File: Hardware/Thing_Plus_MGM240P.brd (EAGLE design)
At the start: 22.9 x 58.4 mm, 176 parts, among them J1 THING_PLUS_LOGICAL, J2 USB Female Type C Connector, J3 QWIIC_RIGHT_ANGLE, J5 MICRO-SDFRICTION, Q1 20V/4.2A/52mΩ/1.4W, U1 MGM240P, U2 XC6222B331MR-G, U3 EFM32GG12B410F1024GL120, U4 MCP73831, U5 MAX17048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

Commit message: Fix air wire
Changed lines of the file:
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@@
 <wire x1="4.1569" y1="15.49" x2="4.0259" y2="15.621" width="0.254" layer="16"/>
 <via x="4.0259" y="15.621" extent="1-16" drill="0.3048"/>
-<via x="0.6604" y="8.0772" extent="1-16" drill="0.3048"/>
+<via x="3.4544" y="6.8072" extent="1-16" drill="0.3048"/>
 <contactref element="C1" pad="1"/>
 <wire x1="4.58" y1="12.7" x2="4.58" y2="15.0669" width="0.254" layer="1"/>
 <wire x1="4.58" y1="15.0669" x2="4.0259" y2="15.621" width="0.254" layer="1"/>
-<wire x1="1.778" y1="7.2517" x2="1.4859" y2="7.2517" width="0.127" layer="16"/>
-<wire x1="1.4859" y1="7.2517" x2="0.6604" y2="8.0772" width="0.127" layer="16"/>
+<wire x1="3.4544" y1="6.8072" x2="2.5654" y2="6.8072" width="0.127" layer="16"/>
+<wire x1="2.5654" y1="6.8072" x2="2.1209" y2="7.2517" width="0.127" layer="16"/>
+<wire x1="1.778" y1="7.2517" x2="2.1209" y2="7.2517" width="0.127" layer="16"/>
 <contactref element="U3" pad="L4"/>
 <contactref element="U3" pad="G3"/>
@@
 <contactref element="R19" pad="2"/>
 <wire x1="6.215" y1="25.4" x2="6.215" y2="26.67" width="0.127" layer="1"/>
-<wire x1="3.81" y1="9.398" x2="1.778" y2="7.2517" width="0" layer="19" extent="16-16"/>
 </signal>
 <signal name="V_USB">

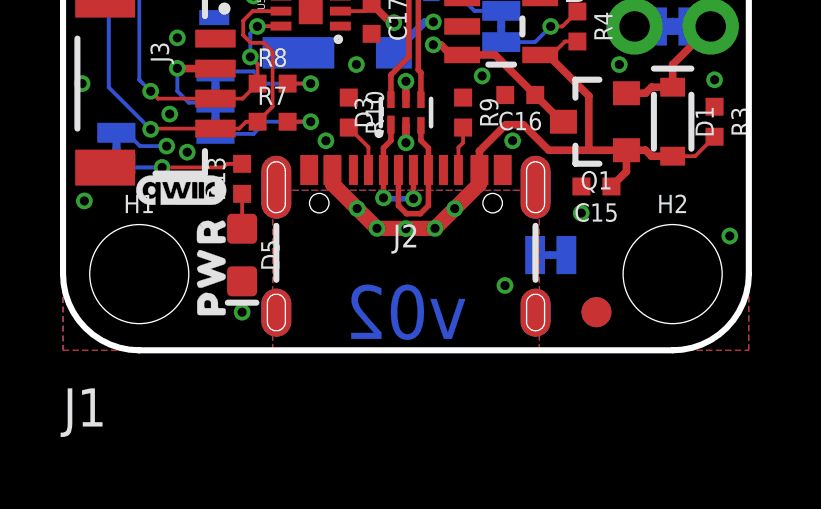
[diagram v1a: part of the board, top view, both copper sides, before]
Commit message: Update revision number to v10
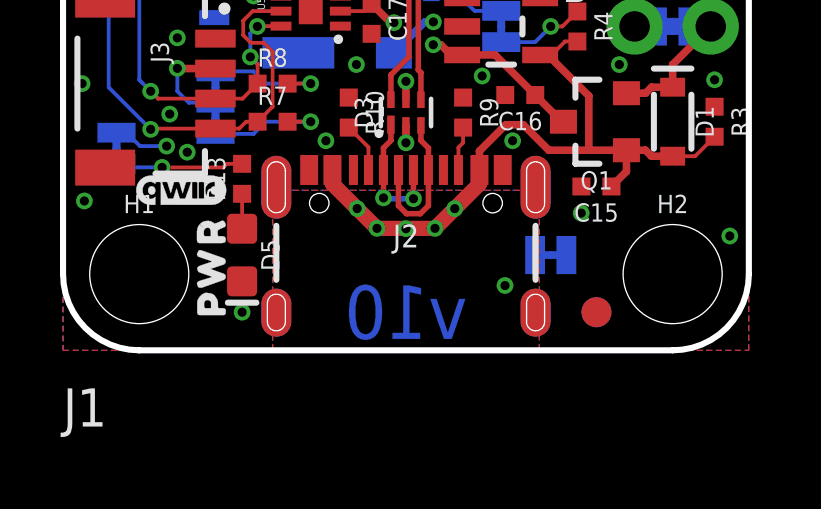
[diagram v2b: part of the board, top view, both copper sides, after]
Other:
- board text added: "v10"
- board text removed: "v02"
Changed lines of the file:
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@@
 <rectangle x1="16.891" y1="57.023" x2="17.272" y2="57.15" layer="41"/>
 <rectangle x1="16.891" y1="56.007" x2="17.272" y2="56.134" layer="41"/>
-<text x="11.43" y="1.27" size="1.778" layer="16" font="vector" ratio="15" rot="MR0" align="center">v02</text>
+<text x="11.43" y="1.27" size="1.778" layer="16" font="vector" ratio="15" rot="MR0" align="center">v10</text>
 <dimension x1="0" y1="0" x2="2.54" y2="0" x3="1.27" y3="-2.54" textsize="1.27" textratio="15" layer="47" unit="inch"/>
 <dimension x1="0" y1="0" x2="11.43" y2="0" x3="5.715" y3="-6.35" textsize="1.27" textratio="15" layer="47" unit="inch"/>

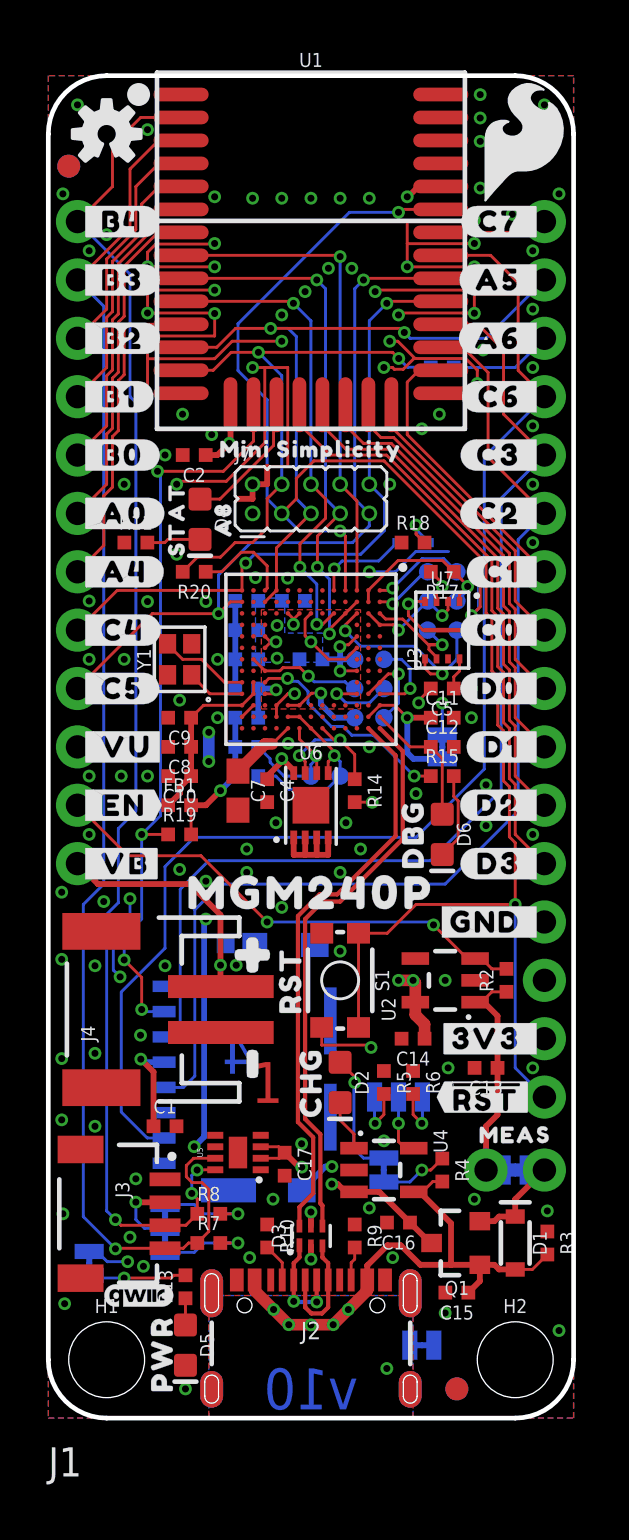
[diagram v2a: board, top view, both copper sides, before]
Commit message: Design review updates
Add "ENIG Finish" to ordering instructions
Add jumpers for rerouting reset line to A0 pin
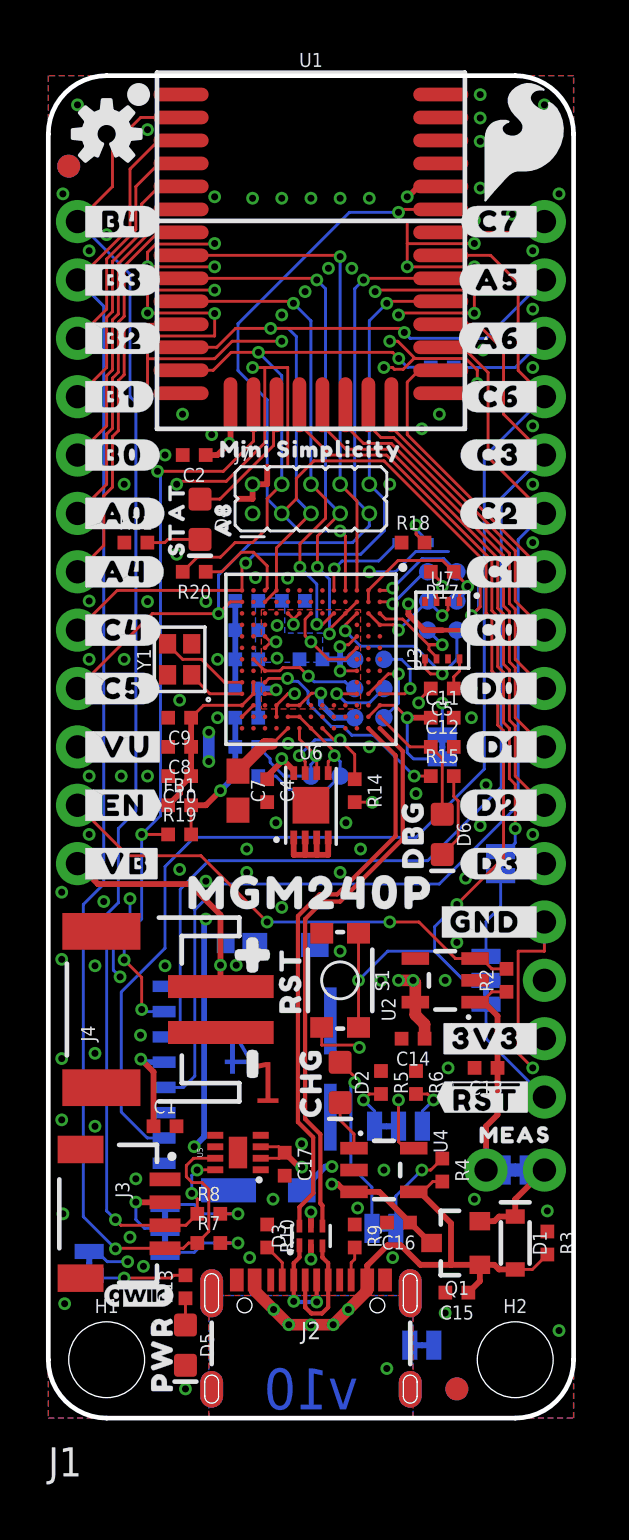
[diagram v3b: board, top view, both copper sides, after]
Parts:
- removed U$47: (no value), output:#_D3#0
- added D3_ISO: JUMPER-SMT_2_NC_TRACE_SILK, SparkFun-Jumpers:SMT-JUMPER_2_NC_TRACE_SILK
- added RST: JUMPER-SMT_3_1-NC_TRACE_SILK, SparkFun-Jumpers:SMT-JUMPER_3_1-NC_TRACE_SILK
- added U$80: (no value), output:#RST#0
- added U$81: (no value), output:#D3#0
- added U$82: (no value), output:#D3#4
- moved CHG 2.54 mm to (14.6, 8.26), turned to 0 degrees
- moved U$60 1.99 mm to (13.7, 8.26), turned to 0 degrees
- moved CHG_I 1.27 mm to (15.2, 12.7)
- moved U$63 1.27 mm to (14.4, 13.3)
- moved U$64 1.27 mm to (16.1, 13.3)
- moved R5 0.13 mm to (14.5, 14.6)
- moved R6 0.13 mm to (16.0, 14.6)
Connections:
- new net A0: D3_ISO.2, J1.24, RST.1
- new net N$28: J1.28, RST.3
- net !RESET!: now also RST.2; no longer J1.28
- net PD03: now also D3_ISO.1; no longer J1.24
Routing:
- net !RESET!: track 73.4 -> 66.8 mm, vias 3 -> 4
- net GND: track 119.5 -> 125.9 mm, vias 137 -> 140
- net A0: track 0.00 -> 5.90 mm
- net N$28: track 0.00 -> 5.09 mm
- net N$3: track 5.51 -> 7.94 mm
- net N$10: track 2.96 -> 4.10 mm
- net N$9: track 2.72 -> 3.74 mm
- net PD03: track 25.8 -> 25.2 mm, vias 0 -> 1
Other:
- board text added: "ENIG Finish"

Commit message: Add Silicon Labs logo
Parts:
- added U$47: (no value), SILICON-LABS-LOGO:SILICON_LABS_LOGO
- moved LOGO1 5.46 mm to (16.9, 54.4)
- moved U$65 0.38 mm to (9.27, 44.5)
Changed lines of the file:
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@@
 <setting verticaltext="up"/>
 </settings>
-<grid distance="0.05" unitdist="inch" unit="inch" style="lines" multiple="1" display="yes" altdistance="0.001" altunitdist="inch" altunit="inch"/>
+<grid distance="0.05" unitdist="inch" unit="inch" style="lines" multiple="1" display="yes" altdistance="0.005" altunitdist="inch" altunit="inch"/>
 <layers>
 <layer number="1" name="Top" color="4" fill="1" visible="yes" active="yes"/>
@@
 <element name="U$21" library="output" package="#GND_#0" value="" x="21.59" y="21.59" smashed="yes"/>
 <element name="U$22" library="output" package="#3V3_#0" value="" x="21.59" y="16.51" smashed="yes"/>
-<element name="LOGO1" library="SparkFun-Aesthetics" package="SFE_LOGO_NAME_FLAME_.1" value="SFE_LOGO_NAME_FLAME.1_INCH" x="11.43" y="54.483" smashed="yes" rot="MR0"/>
+<element name="LOGO1" library="SparkFun-Aesthetics" package="SFE_LOGO_NAME_FLAME_.1" value="SFE_LOGO_NAME_FLAME.1_INCH" x="16.891" y="54.356" smashed="yes" rot="MR0"/>
 <element name="LOGO2" library="SparkFun-Aesthetics" package="QWIIC_3MM" value="QWIIC_LOGO_3MM" x="3.937" y="5.334" smashed="yes"/>
 <element name="LOGO3" library="SparkFun-Aesthetics" package="OSHW-LOGO-S" value="OSHW-LOGOS" x="2.54" y="55.88" smashed="yes"/>
@@
 <attribute name="VALUE" x="17.145" y="45.158" size="0.6096" layer="28" font="vector" ratio="20" rot="MR0" align="top-center"/>
 </element>
-<element name="U$65" library="SEGGER-LOGO" package="SEGGER_LOGO" value="" x="9.65" y="44.45" smashed="yes" rot="MR0"/>
+<element name="U$65" library="SEGGER-LOGO" package="SEGGER_LOGO" value="" x="9.269" y="44.45" smashed="yes" rot="MR0"/>
 <element name="RST" library="SparkFun-Jumpers" package="SMT-JUMPER_3_1-NC_TRACE_SILK" package3d_urn="urn:adsk.eagle:package:39288/1" value="JUMPER-SMT_3_1-NC_TRACE_SILK" x="19.05" y="19.05" smashed="yes" rot="MR270">
 <attribute name="NAME" x="17.907" y="19.05" size="0.6096" layer="26" font="vector" ratio="20" rot="MR270" align="bottom-center"/>
@@
 <element name="U$81" library="output" package="#D3#0" value="" x="18.415" y="19.939" smashed="yes" rot="MR0"/>
 <element name="U$82" library="output" package="#D3#4" value="" x="16.383" y="22.1615" smashed="yes" rot="MR0"/>
+<element name="U$47" library="SILICON-LABS-LOGO" package="SILICON_LABS_LOGO" value="" x="6.096" y="56.007" smashed="yes" rot="MR0"/>
 </elements>
 <signals>
